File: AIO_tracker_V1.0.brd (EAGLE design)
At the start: 47 x 99.8 mm, 52 parts, among them J1 AVR_SPI_PRG_6PTH, Q1 MOSFET-PCHANNELSMD, U2 USD-SOCKETNEW

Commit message: Replaced 0306 smd caps with 0805 smd caps
Replaced the package of the 0306 smd caps with 0805 smd caps of the
larger capacitors (>10uF)
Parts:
- C1, C10, C12, C13, C8, C9: device SparkFun-Passives:0603-CAP -> SparkFun-Passives:0805
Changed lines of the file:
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@@
 <attribute name="VALUE" x="25.19" y="-2.84" size="1.27" layer="27"/>
 </element>
-<element name="C1" library="SparkFun-Passives" package="0603-CAP" value="10uF" x="32.75" y="11" smashed="yes" rot="R90">
+<element name="C1" library="SparkFun-Passives" package="0805" value="10uF" x="32.75" y="11" smashed="yes" rot="R90">
 <attribute name="NAME" x="32.111" y="12.762" size="0.4064" layer="25" font="vector" ratio="25"/>
 </element>
@@
 <attribute name="NAME" x="24.861" y="2.762" size="0.4064" layer="25" font="vector" ratio="25"/>
 </element>
-<element name="C8" library="SparkFun-Passives" package="0603-CAP" value="22uF" x="22" y="1" smashed="yes" rot="R270">
+<element name="C8" library="SparkFun-Passives" package="0805" value="22uF" x="22" y="1" smashed="yes" rot="R270">
 <attribute name="NAME" x="21.611" y="-1.238" size="0.4064" layer="25" font="vector" ratio="25"/>
 </element>
-<element name="C9" library="SparkFun-Passives" package="0603-CAP" value="10uF" x="24" y="-3" smashed="yes" rot="R270">
+<element name="C9" library="SparkFun-Passives" package="0805" value="10uF" x="24" y="-3" smashed="yes" rot="R270">
 <attribute name="NAME" x="24.762" y="-2.111" size="0.4064" layer="25" font="vector" ratio="25" rot="R270"/>
 </element>
@@
 <attribute name="VALUE" x="36.11" y="-2.84" size="1.27" layer="27"/>
 </element>
-<element name="C10" library="SparkFun-Passives" package="0603-CAP" value="10uF" x="35" y="11" smashed="yes" rot="R90">
+<element name="C10" library="SparkFun-Passives" package="0805" value="10uF" x="35" y="11" smashed="yes" rot="R90">
 <attribute name="NAME" x="34.889" y="13.238" size="0.4064" layer="25" font="vector" ratio="25" rot="R180"/>
 </element>
@@
 <attribute name="NAME" x="32.861" y="2.762" size="0.4064" layer="25" font="vector" ratio="25"/>
 </element>
-<element name="C12" library="SparkFun-Passives" package="0603-CAP" value="22uF" x="35" y="1" smashed="yes" rot="R270">
+<element name="C12" library="SparkFun-Passives" package="0805" value="22uF" x="35" y="1" smashed="yes" rot="R270">
 <attribute name="NAME" x="35.361" y="2.762" size="0.4064" layer="25" font="vector" ratio="25"/>
 </element>
-<element name="C13" library="SparkFun-Passives" package="0603-CAP" value="10uF" x="35" y="-3" smashed="yes" rot="R270">
+<element name="C13" library="SparkFun-Passives" package="0805" value="10uF" x="35" y="-3" smashed="yes" rot="R270">
 <attribute name="NAME" x="33.262" y="-1.611" size="0.4064" layer="25" font="vector" ratio="25" rot="R270"/>
 </element>
@@
 <wire x1="42" y1="46.58" x2="42.08" y2="46.5" width="0.254" layer="1"/>
 <wire x1="42" y1="33.111" x2="42.139" y2="33.25" width="0.254" layer="1"/>
-<wire x1="35" y1="1.85" x2="35.285" y2="2.135" width="0.254" layer="1"/>
+<wire x1="35" y1="1.9" x2="35.285" y2="2.135" width="0.254" layer="1"/>
 <wire x1="35.285" y1="2.135" x2="37.61" y2="2.135" width="0.254" layer="1"/>
 <wire x1="34.75" y1="2.1" x2="34.6" y2="2.25" width="0.254" layer="1"/>
@@
 <wire x1="34.75" y1="7.75" x2="34.75" y2="3.5" width="0.3048" layer="1"/>
 <wire x1="34.75" y1="2.25" x2="34.75" y2="2.1" width="0.3048" layer="1"/>
-<wire x1="34.75" y1="2.1" x2="35" y2="1.85" width="0.3048" layer="1"/>
+<wire x1="34.75" y1="2.1" x2="35" y2="1.9" width="0.3048" layer="1"/>
 <wire x1="34.6" y1="2.25" x2="33.15" y2="2.25" width="0.3048" layer="1"/>
 <wire x1="33.15" y1="2.25" x2="32.75" y2="1.85" width="0.3048" layer="1"/>
@@
 <vertex x="-1" y="-18.75"/>
 </polygon>
-<wire x1="35" y1="0.15" x2="35.1" y2="0.25" width="0.254" layer="1"/>
+<wire x1="35" y1="0.1" x2="35.1" y2="0.25" width="0.254" layer="1"/>
 <wire x1="35.1" y1="0.25" x2="35.75" y2="0.25" width="0.254" layer="1"/>
 <wire x1="35.75" y1="0.25" x2="36.25" y2="0.75" width="0.254" layer="1"/>
@@
 <contactref element="U$6" pad="P$2"/>
 <wire x1="39.11" y1="2.135" x2="38.61" y2="2.135" width="0.254" layer="1"/>
-<wire x1="35" y1="10.15" x2="35" y2="9.5625" width="0.254" layer="1"/>
+<wire x1="35" y1="10.1" x2="35" y2="9.5625" width="0.254" layer="1"/>
 <wire x1="36.3775" y1="4.3725" x2="36.5" y2="4.25" width="0.254" layer="1"/>
 <wire x1="36.5" y1="4.25" x2="37.25" y2="4.25" width="0.254" layer="1"/>
@@
 <wire x1="26.7275" y1="8.185" x2="26.5" y2="8.4125" width="0.6096" layer="1"/>
 <wire x1="26.5" y1="8.4125" x2="26.5" y2="10.75" width="0.6096" layer="1"/>
-<wire x1="32.75" y1="10.15" x2="27.1" y2="10.15" width="0.6096" layer="1"/>
-<wire x1="35" y1="10.15" x2="32.75" y2="10.15" width="0.6096" layer="1"/>
+<wire x1="32.75" y1="10.1" x2="27.1" y2="10.15" width="0.6096" layer="1"/>
+<wire x1="35" y1="10.1" x2="32.75" y2="10.1" width="0.6096" layer="1"/>
 <wire x1="35" y1="9.5625" x2="36.3775" y2="8.185" width="0.6096" layer="1"/>
 <wire x1="36.3775" y1="4.3725" x2="36.3775" y2="8.185" width="0.6096" layer="1"/>
@@
 <wire x1="27.19" y1="-0.815" x2="27.19" y2="-1.5" width="0.3048" layer="1"/>
 <wire x1="27.19" y1="-1.5" x2="27.19" y2="-1.56" width="0.3048" layer="1"/>
-<wire x1="22" y1="1.85" x2="24.25" y2="1.85" width="0.4064" layer="1"/>
+<wire x1="22" y1="1.9" x2="24.25" y2="1.85" width="0.4064" layer="1"/>
 <wire x1="21" y1="4.75" x2="19.75" y2="3.5" width="0.4064" layer="16"/>
 <wire x1="20.25" y1="-3.75" x2="20.25" y2="-5.5" width="0.4064" layer="16"/>
-<wire x1="22" y1="1.85" x2="21.9" y2="1.75" width="0.4064" layer="1"/>
+<wire x1="22" y1="1.9" x2="21.9" y2="1.75" width="0.4064" layer="1"/>
 <wire x1="20.25" y1="-3.75" x2="21.25" y2="-2.75" width="0.4064" layer="16"/>
 <wire x1="19.75" y1="-0.75" x2="19.75" y2="3.5" width="0.4064" layer="16"/>
-<wire x1="22" y1="1.85" x2="21.85" y2="2" width="0.4064" layer="1"/>
+<wire x1="22" y1="1.9" x2="21.85" y2="2" width="0.4064" layer="1"/>
 <wire x1="21.85" y1="2" x2="21" y2="2" width="0.4064" layer="1"/>
 <wire x1="21" y1="-2" x2="19.75" y2="-0.75" width="0.4064" layer="16"/>
@@
 <contactref element="IC1" pad="1"/>
 <contactref element="C9" pad="1"/>
-<wire x1="24" y1="-2.15" x2="25.335" y2="-0.815" width="0.3048" layer="1"/>
+<wire x1="24" y1="-2.1" x2="25.335" y2="-0.815" width="0.3048" layer="1"/>
 <wire x1="25.335" y1="-0.815" x2="26.69" y2="-0.815" width="0.3048" layer="1"/>
 </signal>
@@
 <contactref element="IC2" pad="1"/>
 <contactref element="C13" pad="1"/>
-<wire x1="35" y1="-2.15" x2="36.335" y2="-0.815" width="0.254" layer="1"/>
+<wire x1="35" y1="-2.1" x2="36.335" y2="-0.815" width="0.254" layer="1"/>
 <wire x1="36.335" y1="-0.815" x2="37.61" y2="-0.815" width="0.254" layer="1"/>
 </signal>

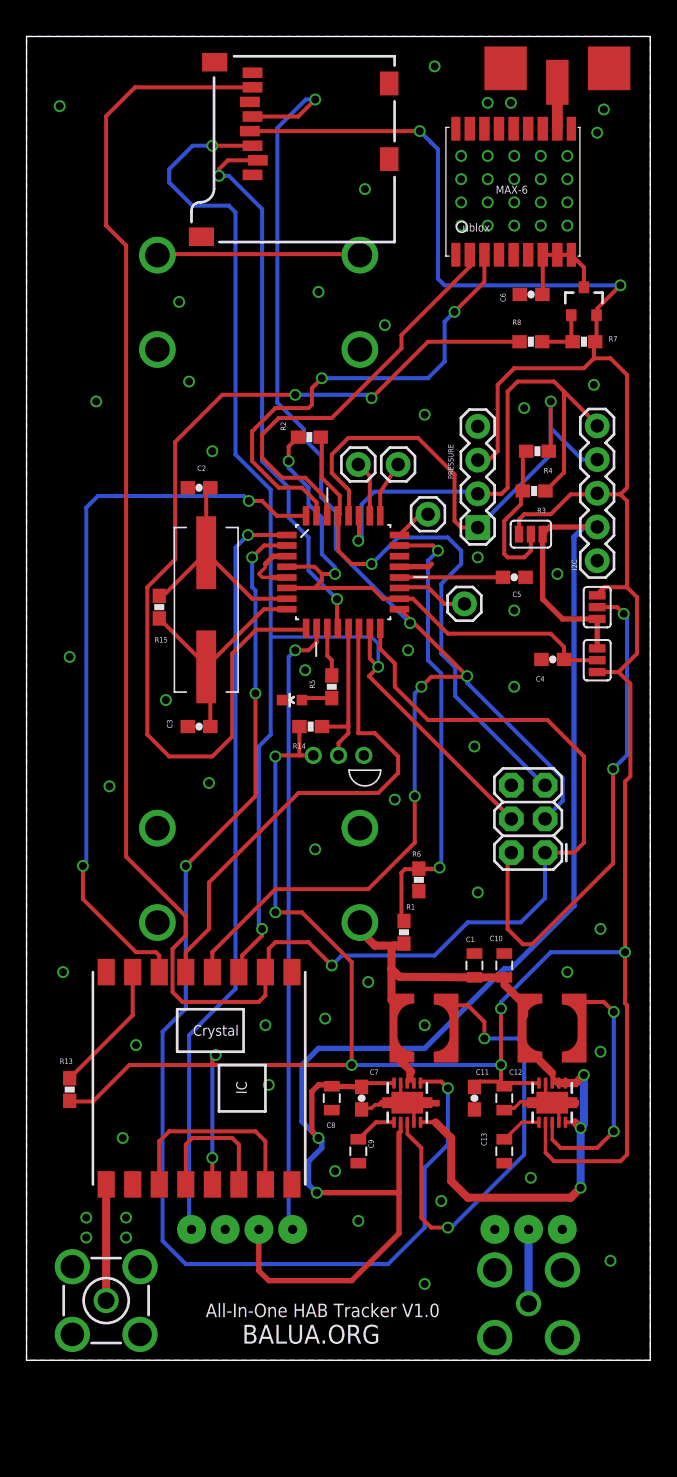
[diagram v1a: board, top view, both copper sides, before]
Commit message: Replaced HX1 Enable, added Soft Serial (A3 and A2)
Replaced HX1 Enable with a non pwm pin, added soft serial (A2 and A3)
silkscreened isolated pins.
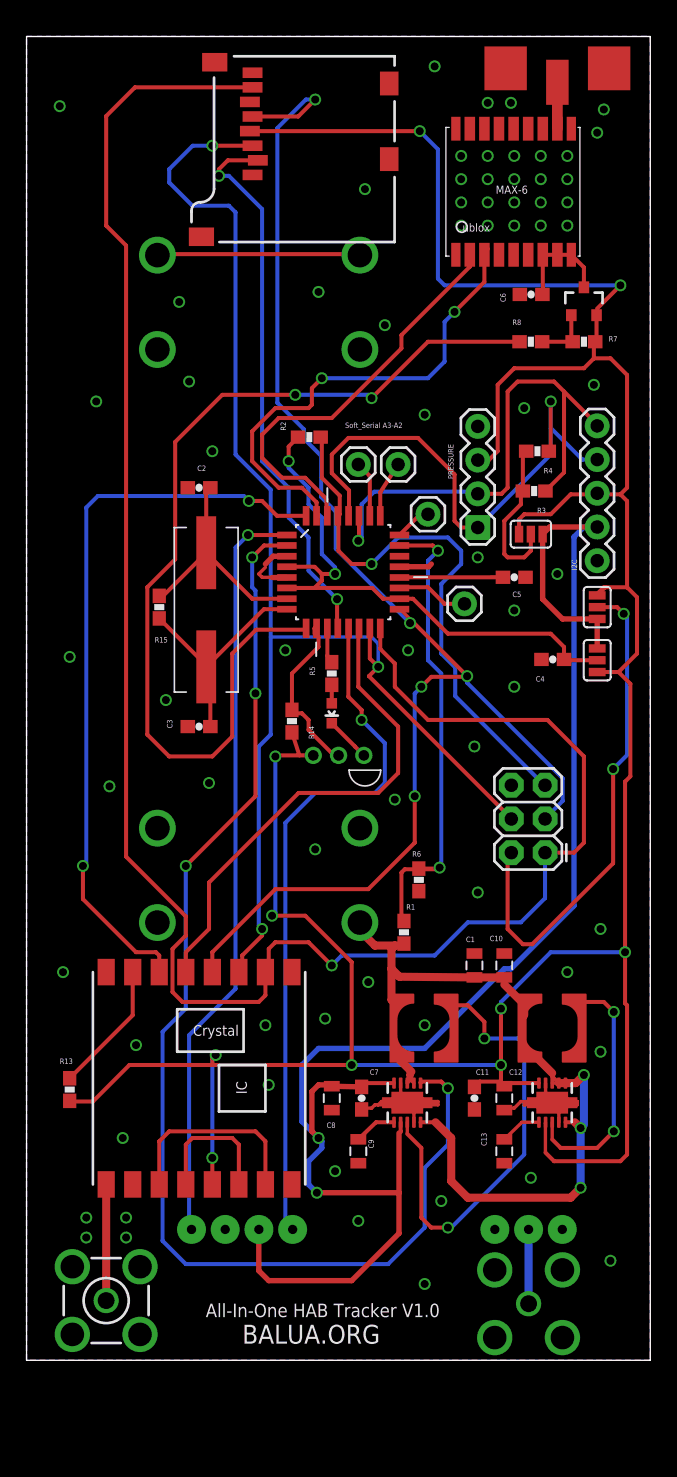
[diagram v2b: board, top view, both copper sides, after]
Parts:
- moved LED1 3.16 mm to (22.0, 30.0), turned to 180 degrees
- moved R14 1.47 mm to (19.0, 29.4), turned to 270 degrees
- moved R5 1.00 mm to (22.0, 33.0)
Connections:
- net 5VEN: now also U1.13; no longer U1.10
- net D4: now also U1.10; no longer U1.13
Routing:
- net 5VEN: track 46.9 -> 52.4 mm
- net GND: track 34.6 -> 38.0 mm
- net LED: track 3.69 -> 2.69 mm
- net N$1: track 2.31 -> 1.40 mm
- net RFM22_NSEL: track 38.0 -> 37.3 mm
- net D4: track 11.9 -> 12.5 mm
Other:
- board text added: "Soft_Serial A3-A2"
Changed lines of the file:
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@@
 <text x="15.25" y="-17.5" size="1.4224" layer="25">BALUA.ORG</text>
 <text x="12.5" y="-15.5" size="1.016" layer="25">All-In-One HAB Tracker V1.0</text>
+<text x="23" y="51.5" size="0.4064" layer="25" font="vector" ratio="25">Soft_Serial A3-A2</text>
 </plain>
 <attributes>
@@
 <attribute name="NAME" x="38.639" y="48.488" size="0.4064" layer="25" font="vector" ratio="25" rot="R180"/>
 </element>
-<element name="LED1" library="SparkFun-LED" package="LED-0603" value="" x="19" y="31" smashed="yes" rot="R90">
-<attribute name="VALUE" x="20.016" y="32.0795" size="0.4064" layer="27" rot="R180"/>
-</element>
-<element name="R5" library="SparkFun-Passives" package="0603-RES" value="1k" x="22" y="32" smashed="yes" rot="R90">
-<attribute name="NAME" x="20.738" y="31.861" size="0.4064" layer="25" font="vector" ratio="25" rot="R90"/>
+<element name="LED1" library="SparkFun-LED" package="LED-0603" value="" x="22" y="30" smashed="yes" rot="R180">
+<attribute name="VALUE" x="20.9205" y="31.016" size="0.4064" layer="27" rot="R270"/>
+</element>
+<element name="R5" library="SparkFun-Passives" package="0603-RES" value="1k" x="22" y="33" smashed="yes" rot="R90">
+<attribute name="NAME" x="20.738" y="32.861" size="0.4064" layer="25" font="vector" ratio="25" rot="R90"/>
 </element>
 <element name="R6" library="SparkFun-Passives" package="0603-RES" value="10k" x="28.56" y="17.45" smashed="yes" rot="R90">
@@
 <attribute name="VALUE" x="36.175" y="42.73" size="1.27" layer="27" rot="R90"/>
 </element>
-<element name="R14" library="SparkFun-Passives" package="0603-RES" value="4.7k" x="20.41" y="29" smashed="yes" rot="R180">
-<attribute name="NAME" x="20.049" y="27.738" size="0.4064" layer="25" font="vector" ratio="25" rot="R180"/>
+<element name="R14" library="SparkFun-Passives" package="0603-RES" value="4.7k" x="19" y="29.41" smashed="yes" rot="R270">
+<attribute name="NAME" x="20.262" y="29.049" size="0.4064" layer="25" font="vector" ratio="25" rot="R270"/>
 </element>
 <element name="I2C" library="SparkFun-Connectors" package="1X05" value="" x="42" y="41.5" smashed="yes" rot="R90">
@@
 <wire x1="33.15" y1="2.25" x2="32.75" y2="1.85" width="0.3048" layer="1"/>
 <wire x1="2.3" y1="0.75" x2="2.25" y2="0.8" width="0.3048" layer="1"/>
-<wire x1="23.5" y1="11.25" x2="19.75" y2="15" width="0.3048" layer="1"/>
-<wire x1="19.75" y1="15" x2="17.75" y2="15" width="0.3048" layer="1"/>
-<via x="17.75" y="15" extent="1-16" drill="0.6"/>
+<wire x1="23.5" y1="11.25" x2="20" y2="14.75" width="0.3048" layer="1"/>
 <wire x1="17.75" y1="15" x2="17.75" y2="26.75" width="0.3048" layer="16"/>
 <wire x1="44.1" y1="12" x2="44.1" y2="8.15" width="0.3048" layer="1"/>
@@
 <wire x1="45" y1="38.75" x2="45" y2="34.5" width="0.3048" layer="1"/>
 <wire x1="20.605" y1="26.83" x2="19.56" y2="26.83" width="0.254" layer="1"/>
-<wire x1="19.56" y1="26.83" x2="19.56" y2="29" width="0.3048" layer="1"/>
+<wire x1="19.56" y1="26.83" x2="19" y2="28.56" width="0.3048" layer="1"/>
 <wire x1="41.75" y1="56.75" x2="41" y2="56" width="0.3048" layer="1"/>
 <wire x1="41" y1="56" x2="35.75" y2="56" width="0.3048" layer="1"/>
@@
 <wire x1="13" y1="-3.5" x2="13" y2="4" width="0.3048" layer="16"/>
 <wire x1="13" y1="4" x2="13.25" y2="4.25" width="0.3048" layer="16"/>
-<wire x1="30" y1="72.5" x2="29.5" y2="73" width="0.3048" layer="16"/>
 <wire x1="15.83" y1="73.87" x2="28.63" y2="73.87" width="0.3048" layer="1"/>
-<wire x1="28.63" y1="73.87" x2="28.75" y2="73.75" width="0.3048" layer="16"/>
-<wire x1="29.5" y1="73" x2="28.75" y2="73.75" width="0.3048" layer="16"/>
+<wire x1="30" y1="72.5" x2="28.63" y2="73.87" width="0.3048" layer="16"/>
 <via x="28.63" y="73.87" extent="1-16" drill="0.6"/>
+<wire x1="17.75" y1="15" x2="17.5" y2="14.75" width="0.3048" layer="16"/>
+<via x="17.5" y="14.75" extent="1-16" drill="0.6"/>
+<wire x1="17.5" y1="14.75" x2="20" y2="14.75" width="0.3048" layer="1"/>
 </signal>
 <signal name="MOSI">
@@
 <via x="30.25" y="-6.75" extent="1-16" drill="0.6"/>
 <via x="33.75" y="76" extent="1-16" drill="0.6"/>
-<via x="20" y="33.25" extent="1-16" drill="0.6"/>
+<via x="18.5" y="34.75" extent="1-16" drill="0.6"/>
+<wire x1="24.415" y1="26.83" x2="23.75" y2="27.495" width="0.3048" layer="1"/>
+<wire x1="23.75" y1="27.495" x2="23.75" y2="27.5" width="0.3048" layer="1"/>
+<wire x1="23.75" y1="27.5" x2="22" y2="29.25" width="0.3048" layer="1"/>
 </signal>
 <signal name="N$4">
@@
 </signal>
 <signal name="5VEN">
-<contactref element="U1" pad="10"/>
 <contactref element="U$3" pad="EN"/>
-<wire x1="20.8534" y1="36.3982" x2="20.8534" y2="35.3534" width="0.3048" layer="1"/>
-<wire x1="20.8534" y1="35.3534" x2="20.25" y2="34.75" width="0.3048" layer="1"/>
-<wire x1="20.25" y1="34.75" x2="19.25" y2="34.75" width="0.3048" layer="1"/>
-<via x="19.25" y="34.75" extent="1-16" drill="0.6"/>
-<wire x1="19.25" y1="34.75" x2="18.75" y2="34.25" width="0.3048" layer="16"/>
-<wire x1="18.75" y1="34.25" x2="18.75" y2="-8.59" width="0.3048" layer="16"/>
-<wire x1="18.75" y1="-8.59" x2="19.05" y2="-8.89" width="0.3048" layer="16"/>
+<contactref element="U1" pad="13"/>
+<wire x1="23.2664" y1="36.3982" x2="23.25" y2="36.3818" width="0.3048" layer="1"/>
+<wire x1="23.25" y1="36.3818" x2="23.25" y2="31.25" width="0.3048" layer="1"/>
+<wire x1="23.25" y1="31.25" x2="24.25" y2="30.25" width="0.3048" layer="1"/>
+<wire x1="24.25" y1="30.25" x2="24.25" y2="29.5" width="0.3048" layer="1"/>
+<via x="24.25" y="29.5" extent="1-16" drill="0.6"/>
+<wire x1="24.25" y1="29.5" x2="26" y2="27.75" width="0.3048" layer="16"/>
+<wire x1="26" y1="27.75" x2="26" y2="24.75" width="0.3048" layer="16"/>
+<wire x1="26" y1="24.75" x2="25.25" y2="24" width="0.3048" layer="16"/>
+<wire x1="25.25" y1="24" x2="20.75" y2="24" width="0.3048" layer="16"/>
+<wire x1="20.75" y1="24" x2="18.5" y2="21.75" width="0.3048" layer="16"/>
+<wire x1="19.05" y1="-8.89" x2="18.5" y2="-8.34" width="0.3048" layer="16"/>
+<wire x1="18.5" y1="-8.34" x2="18.5" y2="21.75" width="0.3048" layer="16"/>
 </signal>
 <signal name="LED">
 <contactref element="U1" pad="11"/>
 <contactref element="R5" pad="2"/>
-<wire x1="21.6662" y1="36.3982" x2="21.6662" y2="34.3338" width="0.3048" layer="1"/>
-<wire x1="21.6662" y1="34.3338" x2="22" y2="34" width="0.3048" layer="1"/>
-<wire x1="22" y1="34" x2="22" y2="32.85" width="0.3048" layer="1"/>
+<wire x1="22" y1="33.85" x2="22" y2="34" width="0.3048" layer="1"/>
+<wire x1="22" y1="34" x2="21.6662" y2="34.3338" width="0.3048" layer="1"/>
+<wire x1="21.6662" y1="34.3338" x2="21.6662" y2="36.3982" width="0.3048" layer="1"/>
 </signal>
 <signal name="N$20">
@@
 </signal>
 <signal name="D4">
-<contactref element="U1" pad="13"/>
 <contactref element="U$9" pad="DQ"/>
 <contactref element="R14" pad="1"/>
-<wire x1="23.2664" y1="36.3982" x2="23.25" y2="36.3818" width="0.254" layer="1"/>
-<wire x1="23.25" y1="36.3818" x2="23.25" y2="29.25" width="0.3048" layer="1"/>
-<wire x1="23.25" y1="29" x2="23.25" y2="28.5" width="0.3048" layer="1"/>
-<wire x1="23.25" y1="28.5" x2="22.51" y2="27.76" width="0.3048" layer="1"/>
-<wire x1="22.51" y1="27.76" x2="22.51" y2="26.83" width="0.3048" layer="1"/>
-<wire x1="21.26" y1="29" x2="23.25" y2="29" width="0.3048" layer="1"/>
-<wire x1="23.25" y1="29" x2="23.25" y2="29.25" width="0.3048" layer="1"/>
+<contactref element="U1" pad="10"/>
+<wire x1="20.8534" y1="36.3982" x2="20.75" y2="36.3982" width="0.4064" layer="1"/>
+<wire x1="20.75" y1="36.3982" x2="20.75" y2="36" width="0.4064" layer="1"/>
+<wire x1="20.75" y1="36" x2="21" y2="35.75" width="0.3048" layer="1"/>
+<wire x1="21" y1="35.75" x2="21" y2="35" width="0.3048" layer="1"/>
+<wire x1="21" y1="35" x2="19" y2="33" width="0.3048" layer="1"/>
+<wire x1="19" y1="33" x2="19" y2="30.26" width="0.3048" layer="1"/>
+<wire x1="22.51" y1="26.83" x2="22.34" y2="27" width="0.3048" layer="1"/>
+<wire x1="22.34" y1="27" x2="22" y2="27" width="0.3048" layer="1"/>
+<wire x1="22" y1="27" x2="20.25" y2="28.75" width="0.3048" layer="1"/>
+<wire x1="20.25" y1="28.75" x2="20.25" y2="29.5" width="0.3048" layer="1"/>
+<wire x1="19" y1="30.26" x2="19" y2="30.25" width="0.3048" layer="1"/>
+<wire x1="19" y1="30.25" x2="19.25" y2="30" width="0.3048" layer="1"/>
+<wire x1="19.25" y1="30" x2="19.75" y2="30" width="0.3048" layer="1"/>
+<wire x1="20.25" y1="29.5" x2="19.75" y2="30" width="0.3048" layer="1"/>
 </signal>
 <signal name="D3">
@@
 <contactref element="R5" pad="1"/>
 <contactref element="LED1" pad="A"/>
-<wire x1="19.75" y1="31" x2="19.9" y2="31.15" width="0.254" layer="1"/>
-<wire x1="19.9" y1="31.15" x2="22" y2="31.15" width="0.3048" layer="1"/>
+<wire x1="22" y1="30.75" x2="22" y2="32.15" width="0.3048" layer="1"/>
 </signal>
 <signal name="N$5">
@@
 <contactref element="U$7" pad="13"/>
 <wire x1="24.0538" y1="36.3982" x2="24" y2="36.3444" width="0.254" layer="1"/>
-<wire x1="24" y1="36.3444" x2="24" y2="28.5" width="0.3048" layer="1"/>
-<wire x1="24" y1="28.5" x2="25.25" y2="28.5" width="0.3048" layer="1"/>
-<wire x1="25.25" y1="28.5" x2="27" y2="26.75" width="0.3048" layer="1"/>
-<wire x1="27" y1="26.75" x2="27" y2="25.5" width="0.3048" layer="1"/>
 <wire x1="27" y1="25.5" x2="25.5" y2="24" width="0.3048" layer="1"/>
 <wire x1="11" y1="12" x2="11" y2="10.5" width="0.3048" layer="1"/>
@@
 <wire x1="12.75" y1="17.25" x2="19.5" y2="24" width="0.3048" layer="1"/>
 <wire x1="19.5" y1="24" x2="25.5" y2="24" width="0.3048" layer="1"/>
+<wire x1="24" y1="36.3444" x2="24" y2="32" width="0.3048" layer="1"/>
+<wire x1="24" y1="32" x2="27" y2="29" width="0.3048" layer="1"/>
+<wire x1="27" y1="29" x2="27" y2="25.5" width="0.3048" layer="1"/>
 </signal>
 <signal name="N$10">
